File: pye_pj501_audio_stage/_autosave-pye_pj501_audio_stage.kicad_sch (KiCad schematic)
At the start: 21 parts, among them T2 PYE_PJ105, U1 EL41, U2 ECH81

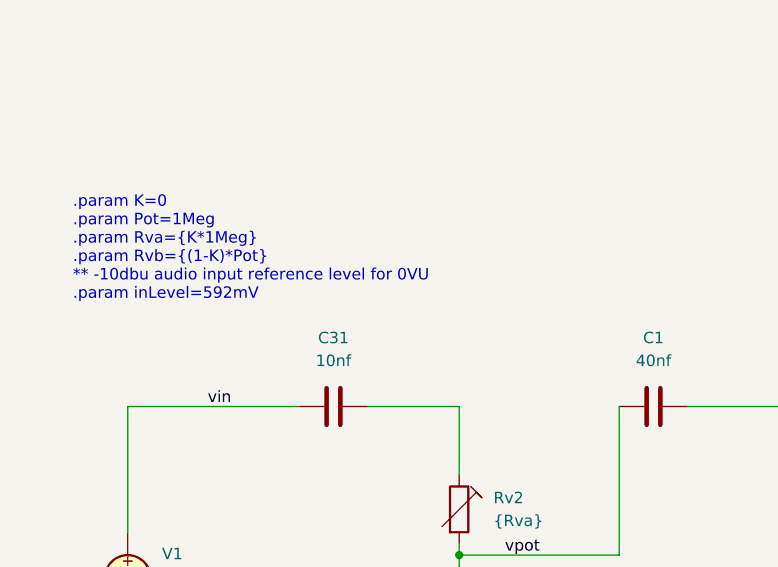
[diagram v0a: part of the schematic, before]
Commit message: added pye sim and updated tx lib
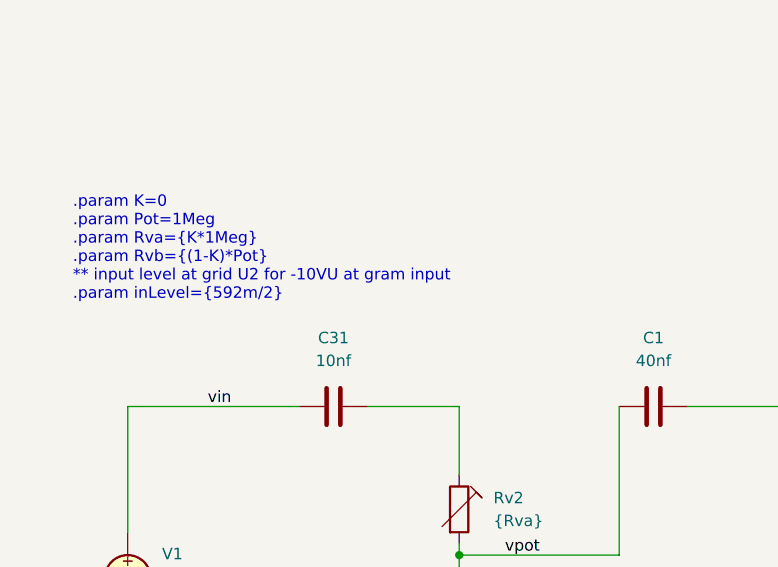
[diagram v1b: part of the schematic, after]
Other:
- note added: ".param K=0 .param Pot=1Meg .param Rva={K*1Meg} .param Rvb={(1-K)*Pot} ** input level at grid U2 for -10VU at gram input .param inLevel={592m/2}"
- note removed: ".param K=0 .param Pot=1Meg .param Rva={K*1Meg} .param Rvb={(1-K)*Pot} ** -10dbu audio input reference level for 0VU .param inLevel=592mV"
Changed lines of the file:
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@@
 		)
 	)
-	(text ".param K=0\n.param Pot=1Meg\n.param Rva={K*1Meg}\n.param Rvb={(1-K)*Pot}\n** -10dbu audio input reference level for 0VU\n.param inLevel=592mV"
+	(text ".param K=0\n.param Pot=1Meg\n.param Rva={K*1Meg}\n.param Rvb={(1-K)*Pot}\n** input level at grid U2 for -10VU at gram input \n.param inLevel={592m/2}"
 		(exclude_from_sim no)
 		(at 16.764 72.644 0)
